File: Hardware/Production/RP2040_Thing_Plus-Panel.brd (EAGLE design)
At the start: 106.7 x 141.7 mm, 1054 parts, among them J1 SWD, J10 USB C, J11 microSD, J14 SWD, J15 Qwiic, J17 USB C, J18 microSD, J2 Qwiic, J21 SWD, J22 Qwiic, J24 USB C, J25 microSD, J28 SWD, J29 Qwiic, J3 Qwiic, J31 USB C, J32 microSD, J35 SWD, J36 Qwiic, J38 USB C, J39 microSD, J42 SWD, J43 Qwiic, J45 USB C, J46 microSD, J49 SWD, J5 USB C, J50 Qwiic, J52 USB C, J53 microSD, J56 SWD, J6 microSD, Q1 20V/4.2A/52mΩ/1.4W, Q2 20V/4.2A/52mΩ/1.4W, Q3 20V/4.2A/52mΩ/1.4W, Q4 20V/4.2A/52mΩ/1.4W, Q5 20V/4.2A/52mΩ/1.4W, Q6 20V/4.2A/52mΩ/1.4W, Q7 20V/4.2A/52mΩ/1.4W, Q8 20V/4.2A/52mΩ/1.4W, U1 W25QXX128MBIT, U10 WS2812-2020, U11 3.3V, U12 MCP73831, U13 W25QXX128MBIT, U14 RP2040, U15 MAX17048, U16 WS2812-2020, U17 3.3V, U18 MCP73831, U19 W25QXX128MBIT, U2 MAX17048, U20 RP2040, U21 MAX17048, U22 WS2812-2020, U23 3.3V, U24 MCP73831, U25 W25QXX128MBIT, U26 RP2040, U27 MAX17048, U28 WS2812-2020, U29 3.3V, U3 MCP73831, U30 MCP73831, U31 W25QXX128MBIT, U32 RP2040, U33 MAX17048, U34 WS2812-2020, U35 3.3V, U36 MCP73831, U37 W25QXX128MBIT, U38 RP2040, U39 MAX17048, U4 W25QXX128MBIT, U40 WS2812-2020, U41 3.3V, U42 MCP73831, U43 W25QXX128MBIT, U44 RP2040, U45 MAX17048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

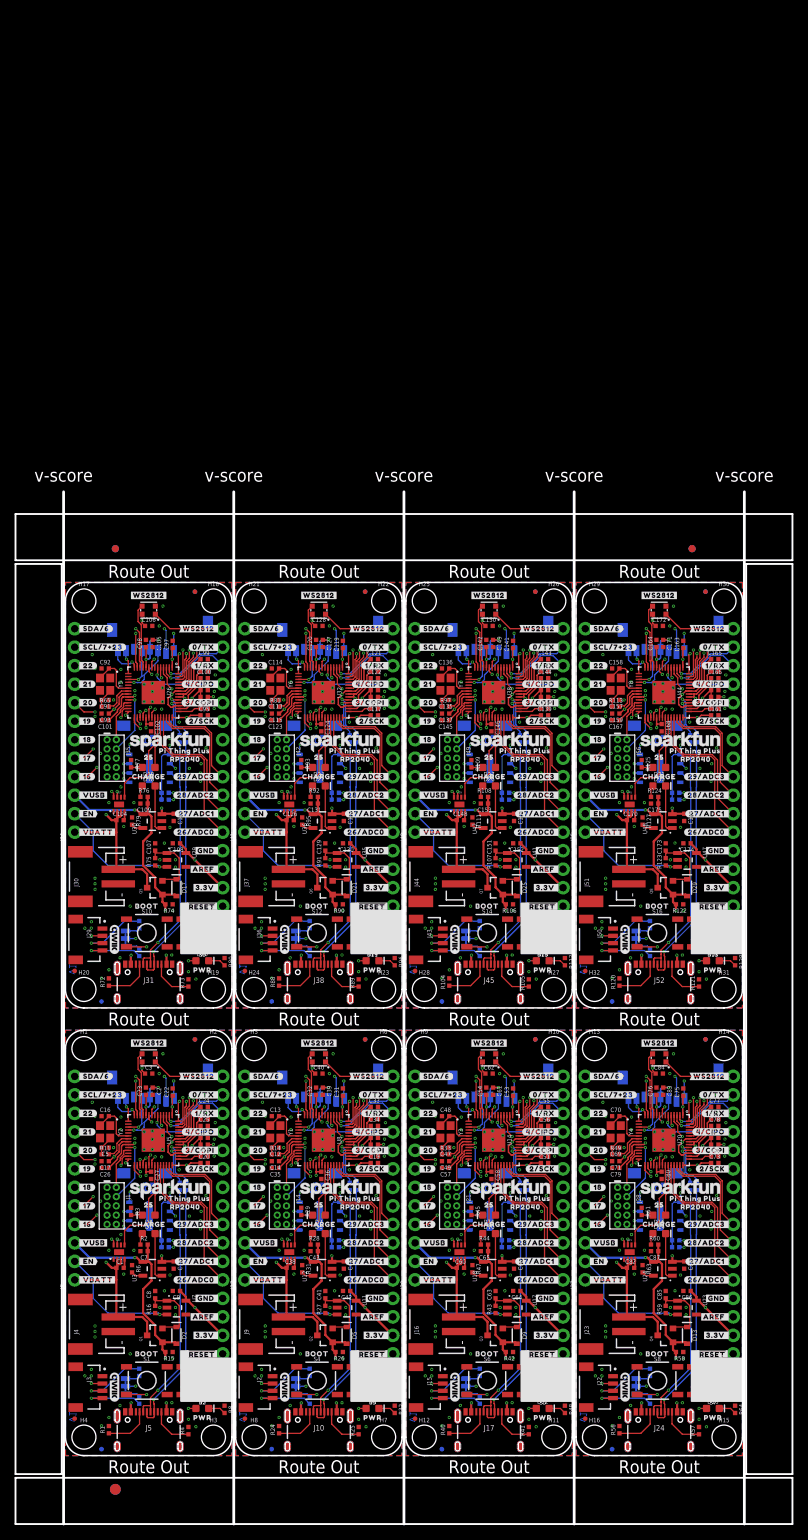
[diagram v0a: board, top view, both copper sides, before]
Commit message: Panel with 2k charge resistor
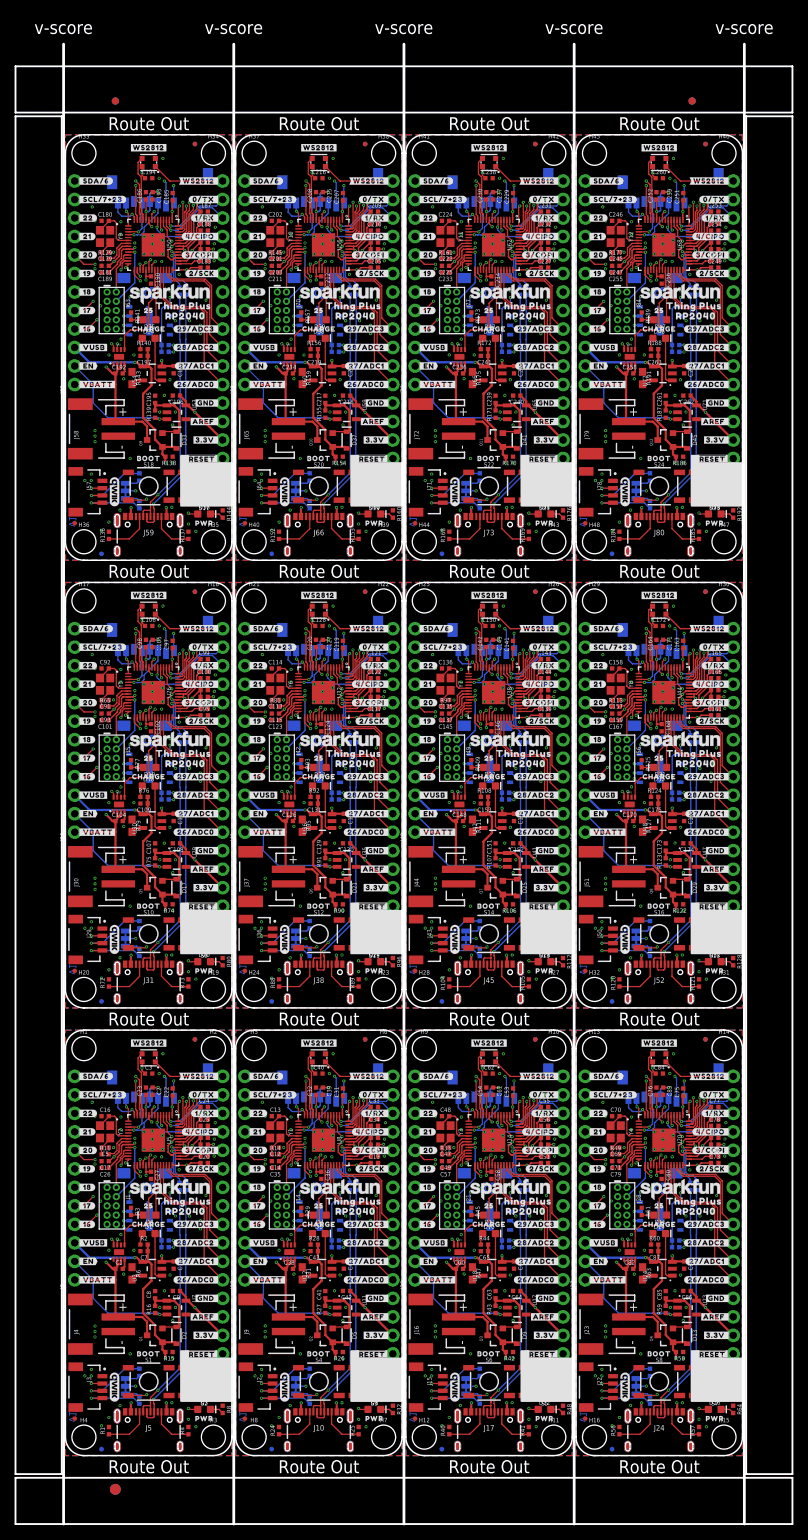
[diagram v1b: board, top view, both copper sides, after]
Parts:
- removed LOGO1, LOGO2, LOGO3, LOGO4, LOGO5, LOGO6, LOGO7, LOGO8: FOUR_LAYER_WARNING, SparkFun-Aesthetics:FOUR_LAYER_WARNING
- added C177, C181, C182, C183, C184, C185, C186, C187, C188, C192, C193, C194, C199, C203, C204, C205, C206, C207, C208, C209, C210, C214, C215, C216, C221, C225, C226, C227, C228, C229, C230, C231, C232, C236, C237, C238, C243, C247, C248, C249, C250, C251, C252, C253, C254, C258, C259, C260: 0.1uF, SparkFun-Capacitors:0402-TIGHT
- added C178, C189, C190, C191, C196, C200, C211, C212, C213, C218, C222, C233, C234, C235, C240, C244, C255, C256, C257, C262: 2.2uF, SparkFun-Capacitors:0402-TIGHT
- added C179, C180, C201, C202, C223, C224, C245, C246: 15pF, SparkFun-Capacitors:0402-TIGHT
- added C195, C217, C239, C261: 1.0uF, SparkFun-Capacitors:0402-TIGHT
- added C197, C198, C219, C220, C241, C242, C263, C264: 4.7uF, SparkFun-Capacitors:0402-TIGHT
- added D33, D37, D41, D45: 1A/23V/620mV, SparkFun-DiscreteSemi:SOD-323
- added D34, D38, D42, D46: Yellow, SparkFun-LED:LED-0603
- added D35, D39, D43, D47: BLUE, SparkFun-LED:LED-0603
- added D36, D40, D44, D48: RED, SparkFun-LED:LED-0603
- added FD33, FD34, FD35, FD36, FD37, FD38, FD39, FD40, FD41, FD42, FD43, FD44, FD45, FD46, FD47, FD48: FIDUCIALUFIDUCIAL, SparkFun-Aesthetics:FIDUCIAL-MICRO
- added H33, H34, H35, H36, H37, H38, H39, H40, H41, H42, H43, H44, H45, H46, H47, H48: STAND-OFF, SparkFun-Hardware:STAND-OFF
- added J57, J64, J71, J78: Qwiic, SparkFun-Connectors:JST04_1MM_RA
- added J58, J65, J72, J79: (no value), SparkFun-Connectors:JST-2-SMD
- added J59, J66, J73, J80: USB C, SparkFun-Connectors:USB-C-16P-4LAYER-ISOLATED
- added J60, J67, J74, J81: microSD, SparkFun-Connectors:MICRO-SD-SOCKET
- added J61, J68, J75, J82: (no value), SparkFun-Connectors:1X16_NO_SILK
- added J62, J69, J76, J83: (no value), SparkFun-Connectors:1X12_NO_SILK
- added J63, J70, J77, J84: SWD, SparkFun-Connectors:2X5-PTH-1.27MM
- added JP10, JP11, JP12, JP9: JUMPER-SMT_3_2-NC_TRACE_SILK, SparkFun-Jumpers:SMT-JUMPER_3_2-NC_TRACE_SILK
- added Q10, Q11, Q12, Q9: 20V/4.2A/52mΩ/1.4W, SparkFun-DiscreteSemi:SOT23-3
- added R129, R134, R140, R141, R144, R145, R150, R156, R157, R160, R161, R166, R172, R173, R176, R177, R182, R188, R189, R192: 1k, SparkFun-Resistors:0402-TIGHT
- added R130, R131, R146, R147, R162, R163, R178, R179: 27, SparkFun-Resistors:0402-TIGHT
- added R132, R133, R148, R149, R164, R165, R180, R181: 2.2k, SparkFun-Resistors:0402-TIGHT
- added R135, R138, R139, R151, R154, R155, R167, R170, R171, R183, R186, R187: 10k, SparkFun-Resistors:0402-TIGHT
- added R136, R137, R152, R153, R168, R169, R184, R185: 5.1k, SparkFun-Resistors:0402-TIGHT
- added R142, R158, R174, R190: 200OHM-0402T-1/16W-1%, SparkFun-Resistors:0402-TIGHT
- added R143, R159, R175, R191: 2.0k, SparkFun-Resistors:0603
- added S17, S18, S19, S20, S21, S22, S23, S24: MOMENTARY-SWITCH-SPST-SMD-5.2MM-TALL, SparkFun-Switches:TACTILE_SWITCH_SMD_5.2MM
- added U$497, U$558, U$619, U$680: (no value), output:#0#TX_#0
- added U$498, U$559, U$620, U$681: (no value), output:#1#RX_#0
- added U$499, U$560, U$621, U$682: (no value), output:#4#CIPO_#0
- added U$500, U$561, U$622, U$683: (no value), output:#3#COPI_#0
- added U$501, U$562, U$623, U$684: (no value), output:#2#SCK_#0
- added U$502, U$563, U$624, U$685: (no value), output:#_SCL#7#23#0
- added U$503, U$564, U$625, U$686: (no value), output:#_SDA#6#0
- added U$504, U$565, U$626, U$687: (no value), output:#29#ADC3_#0
- added U$505, U$566, U$627, U$688: (no value), output:#28#ADC2_#0
- added U$506, U$567, U$628, U$689: (no value), output:#27#ADC1_#0
- added U$507, U$568, U$629, U$690: (no value), output:#26#ADC0_#0
- added U$508, U$569, U$630, U$691: (no value), output:#_VUSB#0
- added U$509, U$570, U$631, U$692: (no value), output:#_EN#0
- added U$510, U$571, U$632, U$693: (no value), output:#_VBATT#0
- added U$511, U$572, U$633, U$694: (no value), output:#GND_#0
- added U$512, U$573, U$634, U$695: (no value), output:#AREF_#0
- added U$513, U$574, U$635, U$696: (no value), output:#3#3V_#0
- added U$514, U$575, U$636, U$697: (no value), output:##RESET##0
- added U$515, U$576, U$637, U$698: (no value), output:#WS2812#0
- added U$516, U$577, U$638, U$699: (no value), SparkFun-Aesthetics:QWIIC_4MM
- added U$517, U$578, U$639, U$700: (no value), SparkFun-Aesthetics:SFE_LOGO_NAME_FLAME_.1
- added U$518, U$579, U$640, U$701: (no value), output:250
- added U$519, U$580, U$641, U$702: (no value), output:CHARGE0
- added U$520, U$581, U$642, U$703: (no value), output:BOOT0
- added U$521, U$582, U$643, U$704: (no value), output:#22_#0
- added U$522, U$583, U$644, U$705: (no value), output:#21_#0
- added U$523, U$584, U$645, U$706: (no value), output:#20_#0
- added U$524, U$585, U$646, U$707: (no value), output:#19_#0
- added U$525, U$586, U$647, U$708: (no value), output:#18_#0
- added U$526, U$587, U$648, U$709: (no value), output:#17_#0
- added U$527, U$588, U$649, U$710: (no value), output:#16_#0
- added U$528, U$589, U$650, U$711: (no value), output:#VUSB_#0
- added U$529, U$590, U$651, U$712: (no value), output:#EN_#0
- added U$530, U$591, U$652, U$713: (no value), output:#VBATT_#0
- added U$531, U$592, U$653, U$714: (no value), output:#SCL_#0
- added U$532, U$593, U$654, U$715: (no value), output:#SDA_#0
- added U$533, U$594, U$655, U$716: (no value), output:#_#RESET##0
- added U$534, U$595, U$656, U$717: (no value), output:#_3#3V#0
- added U$535, U$596, U$657, U$718: (no value), output:#_AREF#0
- added U$536, U$597, U$658, U$719: (no value), output:#_GND#0
- added U$537, U$598, U$659, U$720: (no value), output:#_26#ADC0#0
- added U$538, U$599, U$660, U$721: (no value), output:#_27#ADC1#0
- added U$539, U$600, U$661, U$722: (no value), output:#_28#ADC2#0
- added U$540, U$601, U$662, U$723: (no value), output:#_29#ADC3#0
- added U$541, U$542, U$602, U$603, U$663, U$664, U$724, U$725: (no value), output:#_NC#0
- added U$543, U$604, U$665, U$726: (no value), output:PWR0
- added U$544, U$605, U$666, U$727: (no value), output:#I�C#0
- added U$545, U$606, U$667, U$728: (no value), SparkFun-Aesthetics:SFE_LOGO_NAME_.1
- added U$546, U$607, U$668, U$729: (no value), output:RP2040_1
- added U$547, U$608, U$669, U$730: (no value), output:THING_PLUS_0
- added U$548, U$609, U$670, U$731: (no value), output:RP20401
- added U$549, U$610, U$671, U$732: (no value), output:THING_PLUS0
- added U$550, U$611, U$672: (no value), output:#_16#0
- added U$551, U$612, U$673: (no value), output:#_17#0
- added U$552, U$613, U$674: (no value), output:#_18#0
- added U$553, U$614, U$675: (no value), output:#_19#0
- added U$554, U$615, U$676: (no value), output:#_20#0
- added U$555, U$616, U$677: (no value), output:#_21#0
- added U$556, U$617, U$678: (no value), output:#_22#0
- added U$557, U$618, U$679: (no value), output:#WS2812_#0
- added U49, U55, U61, U67: W25QXX128MBIT, SparkFun-IC-Memory:WSON-8-6X5-SKINNY_CENTERPAD
- added U50, U56, U62, U68: RP2040, RP2040:QFN-56
- added U51, U57, U63, U69: MAX17048, SparkFun-IC-Power:DFN-8
- added U52, U58, U64, U70: WS2812-2020, SparkFun-LED:WS2812-2020
- added U53, U59, U65, U71: 3.3V, SparkFun-IC-Power:SOT23-5
- added U54, U60, U66, U72: MCP73831, SparkFun-IC-Power:SOT23-5
- added Y10, Y11, Y12, Y9: 12MHz, SparkFun-Clocks:CRYSTAL-SMD-2X2.5MM
- R111, R127, R31, R47, R6, R63, R79, R95: value 1k -> 2.0k; device SparkFun-Resistors:0402-TIGHT -> SparkFun-Resistors:0603
- U$100: device output:#18_#0 -> output:#16_#0
- U$101: device output:#17_#0 -> output:#VUSB_#0
- U$102: device output:#16_#0 -> output:#EN_#0
- U$103: device output:#VUSB_#0 -> output:#VBATT_#0
- U$104: device output:#EN_#0 -> output:#SCL_#0
- U$105: device output:#VBATT_#0 -> output:#SDA_#0
- U$106: device output:#SCL_#0 -> output:#_#RESET##0
- U$107: device output:#SDA_#0 -> output:#_3#3V#0
- U$108: device output:#_#RESET##0 -> output:#_AREF#0
- U$109: device output:#_3#3V#0 -> output:#_GND#0
- U$110: device output:#_AREF#0 -> output:#_26#ADC0#0
- U$111: device output:#_GND#0 -> output:#_27#ADC1#0
- U$112: device output:#_26#ADC0#0 -> output:#_28#ADC2#0
- U$113: device output:#_27#ADC1#0 -> output:#_29#ADC3#0
- U$114, U$176: device output:#_28#ADC2#0 -> output:#_NC#0
- U$115: device output:#_29#ADC3#0 -> output:#_NC#0
- U$116: device output:#_NC#0 -> output:PWR0
- U$117, U$178: device output:#_NC#0 -> output:#I�C#0
- U$118: device output:PWR0 -> SparkFun-Aesthetics:SFE_LOGO_NAME_.1
- U$119: device output:#I�C#0 -> output:RP2040_1
- U$120: device output:PI_THING_PLUS0 -> output:THING_PLUS_0
- U$121: device output:RP20400 -> output:RP20401
- U$122: device output:PI_THING_PLUS_0 -> output:THING_PLUS0
- U$123: device output:RP2040_0 -> output:#_16#0
- U$124: device SparkFun-Aesthetics:SFE_LOGO_NAME_.1 -> output:#_17#0
- U$125, U$31: device SparkFun-Aesthetics:ORDERING_INSTRUCTIONS -> output:#_18#0
- U$126: device output:#_16#0 -> output:#_19#0
- U$127: device output:#_17#0 -> output:#_20#0
- U$128: device output:#_18#0 -> output:#_21#0
- U$129: device output:#_19#0 -> output:#_22#0
- U$130: device output:#_20#0 -> output:#WS2812_#0
- U$131: device output:#_21#0 -> output:#0#TX_#0
- U$132: device output:#_22#0 -> output:#1#RX_#0
- U$133: device output:#WS2812_#0 -> output:#4#CIPO_#0
- U$134: device output:#0#TX_#0 -> output:#3#COPI_#0
- U$135: device output:#1#RX_#0 -> output:#2#SCK_#0
- U$136: device output:#4#CIPO_#0 -> output:#_SCL#7#23#0
- U$137: device output:#3#COPI_#0 -> output:#_SDA#6#0
- U$138: device output:#2#SCK_#0 -> output:#29#ADC3_#0
- U$139: device output:#_SCL#7#23#0 -> output:#28#ADC2_#0
- U$140: device output:#_SDA#6#0 -> output:#27#ADC1_#0
- U$141: device output:#29#ADC3_#0 -> output:#26#ADC0_#0
- U$142: device output:#28#ADC2_#0 -> output:#_VUSB#0
- U$143: device output:#27#ADC1_#0 -> output:#_EN#0
- U$144: device output:#26#ADC0_#0 -> output:#_VBATT#0
- U$145: device output:#_VUSB#0 -> output:#GND_#0
- U$146: device output:#_EN#0 -> output:#AREF_#0
- U$147: device output:#_VBATT#0 -> output:#3#3V_#0
- U$148: device output:#GND_#0 -> output:##RESET##0
- U$149: device output:#AREF_#0 -> output:#WS2812#0
- U$150: device output:#3#3V_#0 -> SparkFun-Aesthetics:QWIIC_4MM
- U$151: device output:##RESET##0 -> SparkFun-Aesthetics:SFE_LOGO_NAME_FLAME_.1
- U$152: device output:#WS2812#0 -> output:250
- U$153: device SparkFun-Aesthetics:QWIIC_4MM -> output:CHARGE0
- U$154: device SparkFun-Aesthetics:SFE_LOGO_NAME_FLAME_.1 -> output:BOOT0
- U$155: device output:250 -> output:#22_#0
- U$156: device output:CHARGE0 -> output:#21_#0
- U$157: device output:BOOT0 -> output:#20_#0
- U$158: device output:#22_#0 -> output:#19_#0
- U$159: device output:#21_#0 -> output:#18_#0
- U$160: device output:#20_#0 -> output:#17_#0
- U$161: device output:#19_#0 -> output:#16_#0
- U$162: device output:#18_#0 -> output:#VUSB_#0
- U$163: device output:#17_#0 -> output:#EN_#0
- U$164: device output:#16_#0 -> output:#VBATT_#0
- U$165: device output:#VUSB_#0 -> output:#SCL_#0
- U$166: device output:#EN_#0 -> output:#SDA_#0
- U$167: device output:#VBATT_#0 -> output:#_#RESET##0
- U$168: device output:#SCL_#0 -> output:#_3#3V#0
- U$169: device output:#SDA_#0 -> output:#_AREF#0
- U$170: device output:#_#RESET##0 -> output:#_GND#0
- U$171: device output:#_3#3V#0 -> output:#_26#ADC0#0
- U$172: device output:#_AREF#0 -> output:#_27#ADC1#0
- U$173: device output:#_GND#0 -> output:#_28#ADC2#0
- U$174: device output:#_26#ADC0#0 -> output:#_29#ADC3#0
- U$175, U$237: device output:#_27#ADC1#0 -> output:#_NC#0
- U$177: device output:#_29#ADC3#0 -> output:PWR0
- U$179, U$240: device output:#_NC#0 -> SparkFun-Aesthetics:SFE_LOGO_NAME_.1
- U$180: device output:PWR0 -> output:RP2040_1
- U$181: device output:#I�C#0 -> output:THING_PLUS_0
- U$182: device output:PI_THING_PLUS0 -> output:RP20401
- U$183: device output:RP20400 -> output:THING_PLUS0
- U$184: device output:PI_THING_PLUS_0 -> output:#_16#0
- U$185: device output:RP2040_0 -> output:#_17#0
- U$186: device SparkFun-Aesthetics:SFE_LOGO_NAME_.1 -> output:#_18#0
- U$187: device SparkFun-Aesthetics:ORDERING_INSTRUCTIONS -> output:#_19#0
- U$188: device output:#_16#0 -> output:#_20#0
- U$189: device output:#_17#0 -> output:#_21#0
- U$190: device output:#_18#0 -> output:#_22#0
- U$191: device output:#_19#0 -> output:#WS2812_#0
- U$192: device output:#_20#0 -> output:#0#TX_#0
- U$193: device output:#_21#0 -> output:#1#RX_#0
- U$194: device output:#_22#0 -> output:#4#CIPO_#0
- U$195: device output:#WS2812_#0 -> output:#3#COPI_#0
- U$196: device output:#0#TX_#0 -> output:#2#SCK_#0
- U$197: device output:#1#RX_#0 -> output:#_SCL#7#23#0
- U$198: device output:#4#CIPO_#0 -> output:#_SDA#6#0
- U$199: device output:#3#COPI_#0 -> output:#29#ADC3_#0
- U$200: device output:#2#SCK_#0 -> output:#28#ADC2_#0
- U$201: device output:#_SCL#7#23#0 -> output:#27#ADC1_#0
- U$202: device output:#_SDA#6#0 -> output:#26#ADC0_#0
- U$203: device output:#29#ADC3_#0 -> output:#_VUSB#0
- U$204: device output:#28#ADC2_#0 -> output:#_EN#0
- U$205: device output:#27#ADC1_#0 -> output:#_VBATT#0
- U$206: device output:#26#ADC0_#0 -> output:#GND_#0
- U$207: device output:#_VUSB#0 -> output:#AREF_#0
- U$208: device output:#_EN#0 -> output:#3#3V_#0
- U$209: device output:#_VBATT#0 -> output:##RESET##0
- U$210: device output:#GND_#0 -> output:#WS2812#0
- U$211: device output:#AREF_#0 -> SparkFun-Aesthetics:QWIIC_4MM
- U$212: device output:#3#3V_#0 -> SparkFun-Aesthetics:SFE_LOGO_NAME_FLAME_.1
- U$213: device output:##RESET##0 -> output:250
- U$214: device output:#WS2812#0 -> output:CHARGE0
- U$215: device SparkFun-Aesthetics:QWIIC_4MM -> output:BOOT0
- U$216: device SparkFun-Aesthetics:SFE_LOGO_NAME_FLAME_.1 -> output:#22_#0
- U$217: device output:250 -> output:#21_#0
- U$218: device output:CHARGE0 -> output:#20_#0
- U$219: device output:BOOT0 -> output:#19_#0
- U$220: device output:#22_#0 -> output:#18_#0
- U$221: device output:#21_#0 -> output:#17_#0
- U$222: device output:#20_#0 -> output:#16_#0
- U$223: device output:#19_#0 -> output:#VUSB_#0
- U$224: device output:#18_#0 -> output:#EN_#0
- U$225: device output:#17_#0 -> output:#VBATT_#0
- U$226: device output:#16_#0 -> output:#SCL_#0
- U$227: device output:#VUSB_#0 -> output:#SDA_#0
- U$228: device output:#EN_#0 -> output:#_#RESET##0
- U$229: device output:#VBATT_#0 -> output:#_3#3V#0
- U$230: device output:#SCL_#0 -> output:#_AREF#0
- U$231: device output:#SDA_#0 -> output:#_GND#0
- U$232: device output:#_#RESET##0 -> output:#_26#ADC0#0
- U$233: device output:#_3#3V#0 -> output:#_27#ADC1#0
- U$234: device output:#_AREF#0 -> output:#_28#ADC2#0
- U$235: device output:#_GND#0 -> output:#_29#ADC3#0
- U$236, U$298: device output:#_26#ADC0#0 -> output:#_NC#0
- U$238: device output:#_28#ADC2#0 -> output:PWR0
- U$239: device output:#_29#ADC3#0 -> output:#I�C#0
- U$241, U$302: device output:#_NC#0 -> output:RP2040_1
- U$242: device output:PWR0 -> output:THING_PLUS_0
- U$243: device output:#I�C#0 -> output:RP20401
- U$244: device output:PI_THING_PLUS0 -> output:THING_PLUS0
- U$245: device output:RP20400 -> output:#_16#0
- U$246: device output:PI_THING_PLUS_0 -> output:#_17#0
- U$247: device output:RP2040_0 -> output:#_18#0
- U$248: device SparkFun-Aesthetics:SFE_LOGO_NAME_.1 -> output:#_19#0
- U$249: device SparkFun-Aesthetics:ORDERING_INSTRUCTIONS -> output:#_20#0
- U$250: device output:#_16#0 -> output:#_21#0
- U$251: device output:#_17#0 -> output:#_22#0
- U$252: device output:#_18#0 -> output:#WS2812_#0
- U$253: device output:#_19#0 -> output:#0#TX_#0
- U$254: device output:#_20#0 -> output:#1#RX_#0
- U$255: device output:#_21#0 -> output:#4#CIPO_#0
- U$256: device output:#_22#0 -> output:#3#COPI_#0
- U$257: device output:#WS2812_#0 -> output:#2#SCK_#0
- U$258: device output:#0#TX_#0 -> output:#_SCL#7#23#0
- U$259: device output:#1#RX_#0 -> output:#_SDA#6#0
- U$260: device output:#4#CIPO_#0 -> output:#29#ADC3_#0
- U$261: device output:#3#COPI_#0 -> output:#28#ADC2_#0
- U$262: device output:#2#SCK_#0 -> output:#27#ADC1_#0
- U$263: device output:#_SCL#7#23#0 -> output:#26#ADC0_#0
- U$264: device output:#_SDA#6#0 -> output:#_VUSB#0
- U$265: device output:#29#ADC3_#0 -> output:#_EN#0
- U$266: device output:#28#ADC2_#0 -> output:#_VBATT#0
- U$267: device output:#27#ADC1_#0 -> output:#GND_#0
- U$268: device output:#26#ADC0_#0 -> output:#AREF_#0
- U$269: device output:#_VUSB#0 -> output:#3#3V_#0
- U$270: device output:#_EN#0 -> output:##RESET##0
- U$271: device output:#_VBATT#0 -> output:#WS2812#0
- U$272: device output:#GND_#0 -> SparkFun-Aesthetics:QWIIC_4MM
- U$273: device output:#AREF_#0 -> SparkFun-Aesthetics:SFE_LOGO_NAME_FLAME_.1
- U$274: device output:#3#3V_#0 -> output:250
- U$275: device output:##RESET##0 -> output:CHARGE0
- U$276: device output:#WS2812#0 -> output:BOOT0
- U$277: device SparkFun-Aesthetics:QWIIC_4MM -> output:#22_#0
- U$278: device SparkFun-Aesthetics:SFE_LOGO_NAME_FLAME_.1 -> output:#21_#0
- U$279: device output:250 -> output:#20_#0
- U$280: device output:CHARGE0 -> output:#19_#0
- U$281: device output:BOOT0 -> output:#18_#0
- U$282: device output:#22_#0 -> output:#17_#0
- U$283: device output:#21_#0 -> output:#16_#0
- U$284: device output:#20_#0 -> output:#VUSB_#0
- U$285: device output:#19_#0 -> output:#EN_#0
- U$286: device output:#18_#0 -> output:#VBATT_#0
- U$287: device output:#17_#0 -> output:#SCL_#0
- U$288: device output:#16_#0 -> output:#SDA_#0
- U$289: device output:#VUSB_#0 -> output:#_#RESET##0
- U$29, U$306: device output:PI_THING_PLUS0 -> output:#_16#0
- U$290: device output:#EN_#0 -> output:#_3#3V#0
- U$291: device output:#VBATT_#0 -> output:#_AREF#0
- U$292: device output:#SCL_#0 -> output:#_GND#0
- U$293: device output:#SDA_#0 -> output:#_26#ADC0#0
- U$294: device output:#_#RESET##0 -> output:#_27#ADC1#0
- U$295: device output:#_3#3V#0 -> output:#_28#ADC2#0
- U$296: device output:#_AREF#0 -> output:#_29#ADC3#0
- U$297, U$359: device output:#_GND#0 -> output:#_NC#0
- U$299: device output:#_27#ADC1#0 -> output:PWR0
- U$30, U$307: device output:RP20400 -> output:#_17#0
- U$300: device output:#_28#ADC2#0 -> output:#I�C#0
- U$301: device output:#_29#ADC3#0 -> SparkFun-Aesthetics:SFE_LOGO_NAME_.1
- U$303, U$364: device output:#_NC#0 -> output:THING_PLUS_0
- U$304: device output:PWR0 -> output:RP20401
- U$305: device output:#I�C#0 -> output:THING_PLUS0
- U$308: device output:PI_THING_PLUS_0 -> output:#_18#0
- U$309: device output:RP2040_0 -> output:#_19#0
- U$310: device SparkFun-Aesthetics:SFE_LOGO_NAME_.1 -> output:#_20#0
- U$311: device SparkFun-Aesthetics:ORDERING_INSTRUCTIONS -> output:#_21#0
- U$312: device output:#_16#0 -> output:#_22#0
- U$313: device output:#_17#0 -> output:#WS2812_#0
- U$314: device output:#_18#0 -> output:#0#TX_#0
- U$315: device output:#_19#0 -> output:#1#RX_#0
- U$316: device output:#_20#0 -> output:#4#CIPO_#0
- U$317: device output:#_21#0 -> output:#3#COPI_#0
- U$318: device output:#_22#0 -> output:#2#SCK_#0
- U$319: device output:#WS2812_#0 -> output:#_SCL#7#23#0
- U$320: device output:#0#TX_#0 -> output:#_SDA#6#0
- U$321: device output:#1#RX_#0 -> output:#29#ADC3_#0
- U$322: device output:#4#CIPO_#0 -> output:#28#ADC2_#0
- U$323: device output:#3#COPI_#0 -> output:#27#ADC1_#0
- U$324: device output:#2#SCK_#0 -> output:#26#ADC0_#0
- U$325: device output:#_SCL#7#23#0 -> output:#_VUSB#0
- U$326: device output:#_SDA#6#0 -> output:#_EN#0
- U$327: device output:#29#ADC3_#0 -> output:#_VBATT#0
- U$328: device output:#28#ADC2_#0 -> output:#GND_#0
- U$329: device output:#27#ADC1_#0 -> output:#AREF_#0
- U$330: device output:#26#ADC0_#0 -> output:#3#3V_#0
- U$331: device output:#_VUSB#0 -> output:##RESET##0
- U$332: device output:#_EN#0 -> output:#WS2812#0
- U$333: device output:#_VBATT#0 -> SparkFun-Aesthetics:QWIIC_4MM
- U$334: device output:#GND_#0 -> SparkFun-Aesthetics:SFE_LOGO_NAME_FLAME_.1
- U$335: device output:#AREF_#0 -> output:250
- U$336: device output:#3#3V_#0 -> output:CHARGE0
- U$337: device output:##RESET##0 -> output:BOOT0
- U$338: device output:#WS2812#0 -> output:#22_#0
- U$339: device SparkFun-Aesthetics:QWIIC_4MM -> output:#21_#0
- U$340: device SparkFun-Aesthetics:SFE_LOGO_NAME_FLAME_.1 -> output:#20_#0
- U$341: device output:250 -> output:#19_#0
- U$342: device output:CHARGE0 -> output:#18_#0
- U$343: device output:BOOT0 -> output:#17_#0
- U$344: device output:#22_#0 -> output:#16_#0
- U$345: device output:#21_#0 -> output:#VUSB_#0
- U$346: device output:#20_#0 -> output:#EN_#0
- U$347: device output:#19_#0 -> output:#VBATT_#0
- U$348: device output:#18_#0 -> output:#SCL_#0
- U$349: device output:#17_#0 -> output:#SDA_#0
- U$350: device output:#16_#0 -> output:#_#RESET##0
- U$351: device output:#VUSB_#0 -> output:#_3#3V#0
- U$352: device output:#EN_#0 -> output:#_AREF#0
- U$353: device output:#VBATT_#0 -> output:#_GND#0
- U$354: device output:#SCL_#0 -> output:#_26#ADC0#0
- U$355: device output:#SDA_#0 -> output:#_27#ADC1#0
- U$356: device output:#_#RESET##0 -> output:#_28#ADC2#0
- U$357: device output:#_3#3V#0 -> output:#_29#ADC3#0
- U$358, U$420: device output:#_AREF#0 -> output:#_NC#0
- U$360: device output:#_26#ADC0#0 -> output:PWR0
- U$361: device output:#_27#ADC1#0 -> output:#I�C#0
- U$362: device output:#_28#ADC2#0 -> SparkFun-Aesthetics:SFE_LOGO_NAME_.1
- U$363: device output:#_29#ADC3#0 -> output:RP2040_1
- U$365, U$426: device output:#_NC#0 -> output:RP20401
- U$366: device output:PWR0 -> output:THING_PLUS0
- U$367: device output:#I�C#0 -> output:#_16#0
- U$368: device output:PI_THING_PLUS0 -> output:#_17#0
- U$369: device output:RP20400 -> output:#_18#0
- U$370: device output:PI_THING_PLUS_0 -> output:#_19#0
- U$371: device output:RP2040_0 -> output:#_20#0
- U$372: device SparkFun-Aesthetics:SFE_LOGO_NAME_.1 -> output:#_21#0
- U$373: device SparkFun-Aesthetics:ORDERING_INSTRUCTIONS -> output:#_22#0
- U$374: device output:#_16#0 -> output:#WS2812_#0
- U$375: device output:#_17#0 -> output:#0#TX_#0
- U$376: device output:#_18#0 -> output:#1#RX_#0
- U$377: device output:#_19#0 -> output:#4#CIPO_#0
- U$378: device output:#_20#0 -> output:#3#COPI_#0
- U$379: device output:#_21#0 -> output:#2#SCK_#0
- U$380: device output:#_22#0 -> output:#_SCL#7#23#0
- U$381: device output:#WS2812_#0 -> output:#_SDA#6#0
- U$382: device output:#0#TX_#0 -> output:#29#ADC3_#0
- U$383: device output:#1#RX_#0 -> output:#28#ADC2_#0
- U$384: device output:#4#CIPO_#0 -> output:#27#ADC1_#0
- U$385: device output:#3#COPI_#0 -> output:#26#ADC0_#0
- U$386: device output:#2#SCK_#0 -> output:#_VUSB#0
- U$387: device output:#_SCL#7#23#0 -> output:#_EN#0
- U$388: device output:#_SDA#6#0 -> output:#_VBATT#0
- U$389: device output:#29#ADC3_#0 -> output:#GND_#0
- U$390: device output:#28#ADC2_#0 -> output:#AREF_#0
- U$391: device output:#27#ADC1_#0 -> output:#3#3V_#0
- U$392: device output:#26#ADC0_#0 -> output:##RESET##0
- U$393: device output:#_VUSB#0 -> output:#WS2812#0
- U$394: device output:#_EN#0 -> SparkFun-Aesthetics:QWIIC_4MM
- U$395: device output:#_VBATT#0 -> SparkFun-Aesthetics:SFE_LOGO_NAME_FLAME_.1
- U$396: device output:#GND_#0 -> output:250
- U$397: device output:#AREF_#0 -> output:CHARGE0
- U$398: device output:#3#3V_#0 -> output:BOOT0
- U$399: device output:##RESET##0 -> output:#22_#0
- U$400: device output:#WS2812#0 -> output:#21_#0
- U$401: device SparkFun-Aesthetics:QWIIC_4MM -> output:#20_#0
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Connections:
- net SDIO_DAT1/AUD_IN renamed SDIO_DAT1
- net SDIO_DAT1/AUD_IN1 renamed SDIO_DAT3
- net SDIO_DAT1/AUD_IN2 renamed SDIO_DAT5
- net SDIO_DAT1/AUD_IN3 renamed SDIO_DAT7
- net SDIO_DAT1/AUD_IN4 renamed SDIO_DAT9
- net SDIO_DAT1/AUD_IN5 renamed SDIO_DAT11
- net SDIO_DAT1/AUD_IN6 renamed SDIO_DAT13
- net SDIO_DAT1/AUD_IN7 renamed SDIO_DAT15
- net SDIO_DAT2/AUD_OUT renamed SDIO_DAT2
- net SDIO_DAT2/AUD_OUT1 renamed SDIO_DAT4
- net SDIO_DAT2/AUD_OUT2 renamed SDIO_DAT6
- net SDIO_DAT2/AUD_OUT3 renamed SDIO_DAT8
- net SDIO_DAT2/AUD_OUT4 renamed SDIO_DAT10
- net SDIO_DAT2/AUD_OUT5 renamed SDIO_DAT12
- net SDIO_DAT2/AUD_OUT6 renamed SDIO_DAT14
- net SDIO_DAT2/AUD_OUT7 renamed SDIO_DAT16
- removed net N$102 (its old number): U38.16
- removed net N$104 (its old number): U38.7
- removed net N$13 (its old number): U5.7
- removed net N$24 (its old number): U5.16
- removed net N$27 (its old number): U8.16
- removed net N$29 (its old number): U8.7
- removed net N$42 (its old number): U14.16
- removed net N$44 (its old number): U14.7
- removed net N$57 (its old number): U20.16
- removed net N$59 (its old number): U20.7
- removed net N$72 (its old number): U26.16
- removed net N$74 (its old number): U26.7
- removed net N$87 (its old number): U32.16
- removed net N$89 (its old number): U32.7
- new net !RESET!10: U62.26
- new net !RESET!11: U68.26
- new net !RESET!8: U50.26
- new net !RESET!9: U56.26
- new net !RESET10: J75.1, J77.10, S21.3
- new net !RESET11: J82.1, J84.10, S23.3
- new net !RESET8: J61.1, J63.10, S17.3
- new net !RESET9: J68.1, J70.10, S19.3
- new net 1.1V10: C231.1, C232.1, C233.1, U62.23, U62.45, U62.50
- new net 1.1V11: C253.1, C254.1, C255.1, U68.23, U68.45, U68.50
- new net 1.1V8: C187.1, C188.1, C189.1, U50.23, U50.45, U50.50
- new net 1.1V9: C209.1, C210.1, C211.1, U56.23, U56.45, U56.50
- new net 3.3V10: C221.1, C222.1, C225.1, C226.1, C227.1, C228.1, C229.1, C230.1, C234.1, C237.1, C238.1, C240.1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
- new net 3.3V11: C243.1, C244.1, C247.1, C248.1, C249.1, C250.1, C251.1, C252.1, C256.1, C259.1, C260.1, C262.1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
- new net 3.3V8: C177.1, C178.1, C181.1, C182.1, C183.1, C184.1, C185.1, C186.1, C190.1, C193.1, C194.1, C196.1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
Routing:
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- added copper zone on layer 15, net 3.3V10
- added copper zone on layer 15, net 3.3V11
- added copper zone on layer 15, net 3.3V8
- added copper zone on layer 15, net 3.3V9
- added copper zone on layer 1, net GND10
- added copper zone on layer 16, net GND10
- added copper zone on layer 2, net GND10
- added copper zone on layer 1, net GND11
- added copper zone on layer 16, net GND11
- added copper zone on layer 2, net GND11
- added copper zone on layer 1, net GND8
- added copper zone on layer 16, net GND8
- added copper zone on layer 2, net GND8
- added copper zone on layer 1, net GND9
- added copper zone on layer 16, net GND9
- added copper zone on layer 2, net GND9
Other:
- board size 106.7 x 141.7 mm -> 106.7 x 203.2 mm
- board text removed: "Units in inches"

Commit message: Panelize v11
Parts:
- added TP1, TP10, TP11, TP12, TP13, TP14, TP15, TP16, TP17, TP18, TP19, TP2, TP20, TP21, TP22, TP23, TP24, TP25, TP26, TP27, TP28, TP29, TP3, TP30, TP31, TP32, TP33, TP34, TP35, TP36, TP4, TP5, TP6, TP7, TP8, TP9: (no value), SparkFun-Connectors:PAD.03X.04
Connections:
- removed net !RESET: J1.10, J7.1, S2.3
- removed net !RESET1: J12.1, J14.10, S3.3
- removed net !RESET10: J75.1, J77.10, S21.3
- removed net !RESET11: J82.1, J84.10, S23.3
- removed net !RESET2: J19.1, J21.10, S5.3
- removed net !RESET3: J26.1, J28.10, S7.3
- removed net !RESET4: J33.1, J35.10, S9.3
- removed net !RESET5: J40.1, J42.10, S11.3
- removed net !RESET6: J47.1, J49.10, S13.3
- removed net !RESET7: J54.1, J56.10, S15.3
- removed net !RESET8: J61.1, J63.10, S17.3
- removed net !RESET9: J68.1, J70.10, S19.3
- net !RESET!: now also J1.10, J7.1, S2.3, TP3.P$1
- net !RESET!1: now also J12.1, J14.10, S3.3, TP6.P$1
- net !RESET!10: now also J75.1, J77.10, S21.3, TP33.P$1
- net !RESET!11: now also J82.1, J84.10, S23.3, TP36.P$1
- net !RESET!2: now also J19.1, J21.10, S5.3, TP9.P$1
- net !RESET!3: now also J26.1, J28.10, S7.3, TP12.P$1
- net !RESET!4: now also J33.1, J35.10, S9.3, TP15.P$1
- net !RESET!5: now also J40.1, J42.10, S11.3, TP18.P$1
- net !RESET!6: now also J47.1, J49.10, S13.3, TP21.P$1
- net !RESET!7: now also J54.1, J56.10, S15.3, TP24.P$1
- net !RESET!8: now also J61.1, J63.10, S17.3, TP27.P$1
- net !RESET!9: now also J68.1, J70.10, S19.3, TP30.P$1
- net SWDCK: now also TP1.P$1
- net SWDCK1: now also TP4.P$1
- net SWDCK10: now also TP31.P$1
- net SWDCK11: now also TP34.P$1
- net SWDCK2: now also TP7.P$1
- net SWDCK3: now also TP10.P$1
- net SWDCK4: now also TP13.P$1
- net SWDCK5: now also TP16.P$1
- net SWDCK6: now also TP19.P$1
- net SWDCK7: now also TP22.P$1
- net SWDCK8: now also TP25.P$1
- net SWDCK9: now also TP28.P$1
- net SWDIO: now also TP2.P$1
- net SWDIO1: now also TP5.P$1
- net SWDIO10: now also TP32.P$1
- net SWDIO11: now also TP35.P$1
- net SWDIO2: now also TP8.P$1
- net SWDIO3: now also TP11.P$1
- net SWDIO4: now also TP14.P$1
- net SWDIO5: now also TP17.P$1
- net SWDIO6: now also TP20.P$1
- net SWDIO7: now also TP23.P$1
- net SWDIO8: now also TP26.P$1
- net SWDIO9: now also TP29.P$1
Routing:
- net !RESET!6: track 0.00 -> 47.1 mm, vias 0 -> 2
- net !RESET!4: track 0.00 -> 47.1 mm, vias 0 -> 2
- net !RESET!2: track 0.00 -> 47.1 mm, vias 0 -> 2
- net !RESET!7: track 0.00 -> 47.1 mm, vias 0 -> 2
- net !RESET!5: track 0.00 -> 47.1 mm, vias 0 -> 2
- net !RESET!10: track 0.00 -> 47.1 mm, vias 0 -> 2
- net !RESET!: track 0.00 -> 47.1 mm, vias 0 -> 2
- net !RESET!3: track 0.00 -> 47.1 mm, vias 0 -> 2
- net !RESET!9: track 0.00 -> 47.1 mm, vias 0 -> 2
- net !RESET!8: track 0.00 -> 47.1 mm, vias 0 -> 2
- net !RESET!1: track 0.00 -> 47.1 mm, vias 0 -> 2
- net !RESET!11: track 0.00 -> 47.1 mm, vias 0 -> 2
- net !RESET4: track 33.3 -> 0.00 mm, vias 1 -> 0
- net !RESET9: track 33.3 -> 0.00 mm, vias 1 -> 0
- net !RESET8: track 33.3 -> 0.00 mm, vias 1 -> 0
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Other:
- board text added: "v11"
- board text removed: "v10"

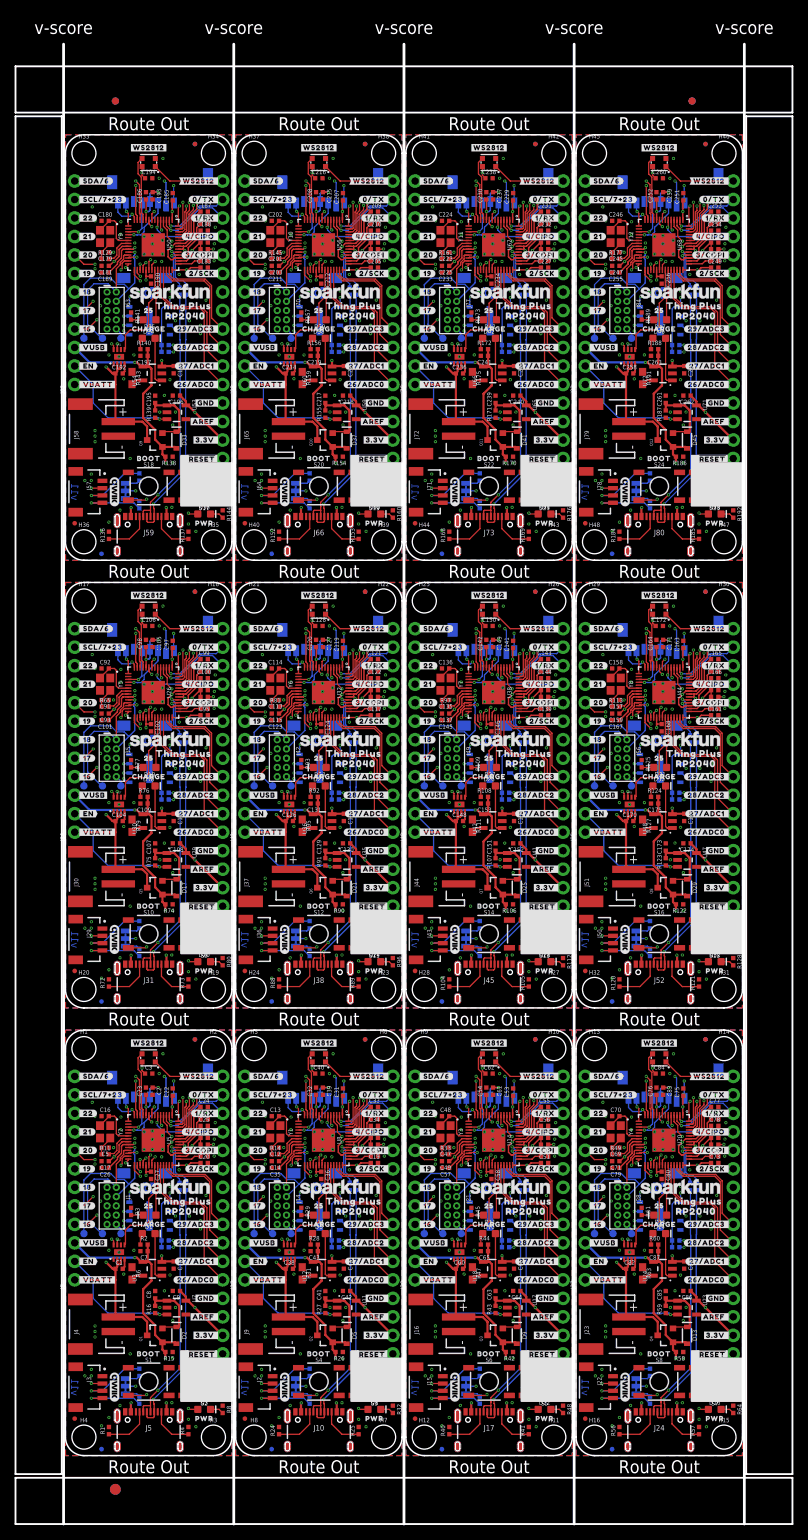
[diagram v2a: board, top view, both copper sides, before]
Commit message: Add RP2040 Logo
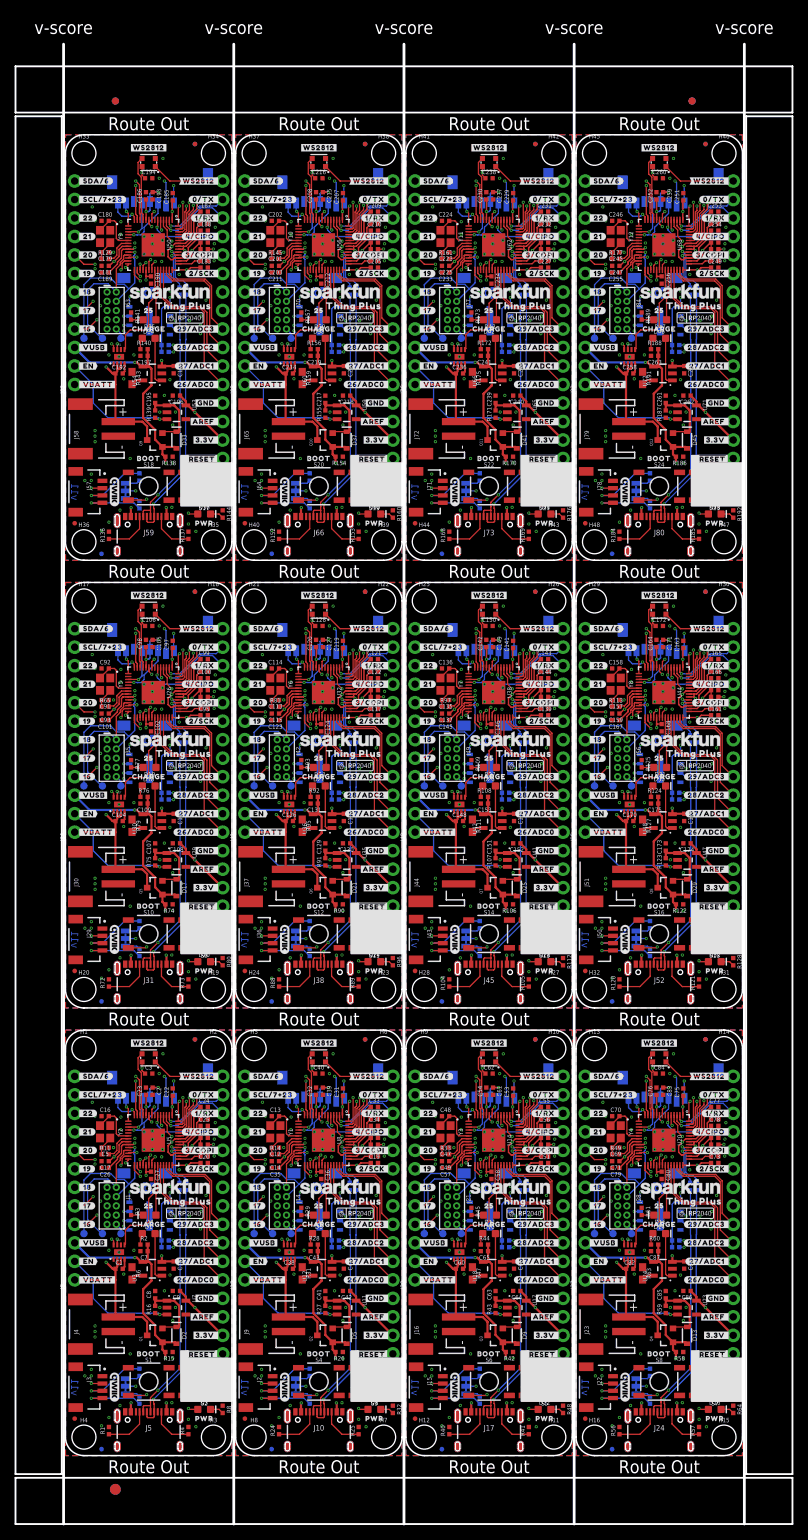
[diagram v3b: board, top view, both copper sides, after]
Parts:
- U$119, U$180, U$241, U$302, U$363, U$424, U$485, U$546, U$607, U$668, U$729: device output:RP2040_1 -> output:THING_PLUS_0
- U$120, U$181, U$242, U$303, U$364, U$425, U$486, U$547, U$608, U$669, U$730: device output:THING_PLUS_0 -> output:THING_PLUS0
- U$121, U$182, U$243, U$304, U$365, U$426, U$487, U$548, U$609, U$670, U$731: device output:RP20401 -> RP2040:RP2040_20
- U$122, U$183, U$244, U$305, U$366, U$427, U$488, U$549, U$610, U$671, U$732: device output:THING_PLUS0 -> RP2040:RP2040_10
- U$29: device output:#_16#0 -> RP2040:RP2040_10
- U$30: device output:#_17#0 -> RP2040:RP2040_20
- U$31: device output:#_18#0 -> output:#_16#0
- U$43: device output:RP20401 -> output:#_17#0
- U$46: device output:RP2040_1 -> output:#_18#0
- moved U$30 28.5 mm to (5.71, 13.3), flipped to the bottom
- moved U$43 27.5 mm to (25.0, 34.3), flipped to the top
- moved U$303 21.0 mm to (6.48, 77.9), flipped to the bottom
- moved U$364 21.0 mm to (29.8, 77.9), flipped to the bottom
- moved U$425 21.0 mm to (53.2, 77.9), flipped to the bottom
- moved U$547 21.0 mm to (6.48, 139.3), flipped to the bottom
- moved U$608 21.0 mm to (29.8, 139.3), flipped to the bottom
- moved U$669 21.0 mm to (53.2, 139.3), flipped to the bottom
- moved U$120 21.0 mm to (29.8, 16.4), flipped to the bottom
- moved U$181 21.0 mm to (53.2, 16.4), flipped to the bottom
- moved U$486 21.0 mm to (76.6, 77.9), flipped to the bottom
- moved U$730 21.0 mm to (76.6, 139.3), flipped to the bottom
- moved U$242 21.0 mm to (76.6, 16.4), flipped to the bottom
- moved U$549 19.6 mm to (16.4, 156.2), flipped to the top
- moved U$610 19.6 mm to (39.8, 156.2), flipped to the top
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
